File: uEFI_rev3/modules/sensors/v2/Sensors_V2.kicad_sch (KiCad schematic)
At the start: 12 parts, among them J1 Conn_01x05_Female, U1 LM321, U2 LM321

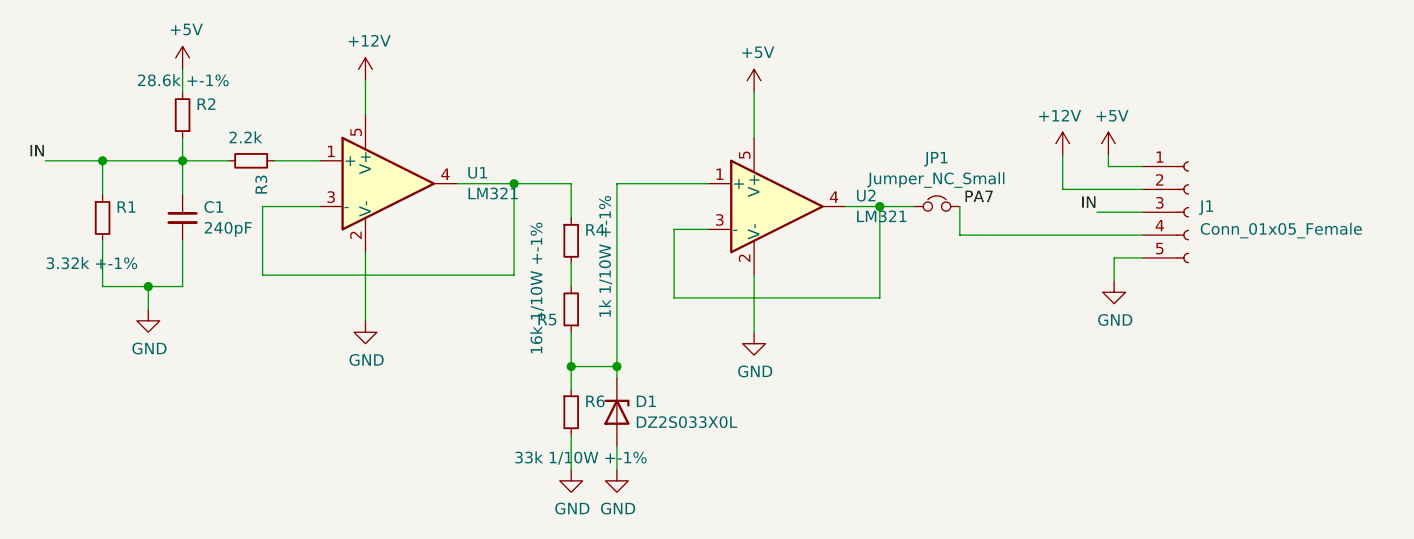
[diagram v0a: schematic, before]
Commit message: move old boards to __old
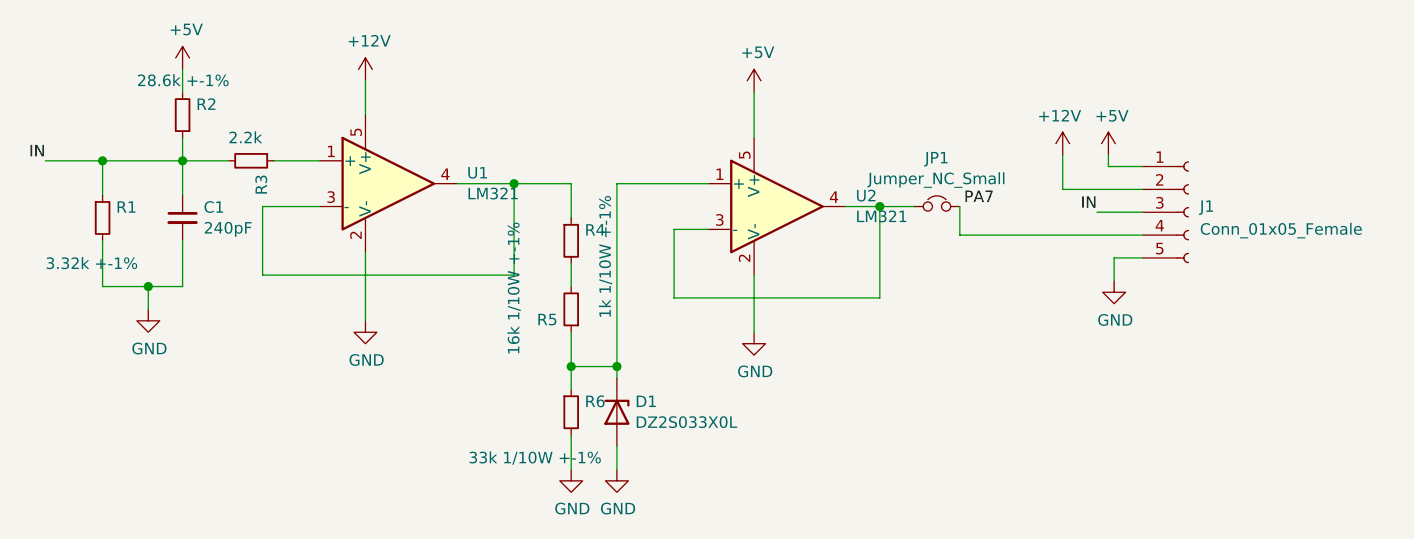
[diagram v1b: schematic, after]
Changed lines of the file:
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@@
-(kicad_sch (version 20210126) (generator eeschema)
+(kicad_sch (version 20210621) (generator eeschema)
   (paper "A4")
   (junction (at 82.55 82.55) (diameter 1.016) (color 0 0 0 0))
@@
       (effects (font (size 1.27 1.27)) (justify left))
     )
-    (property "Value" "16k 1/10W +-1%" (id 1) (at 130.81 104.14 90)
+    (property "Value" "16k 1/10W +-1%" (id 1) (at 128.27 104.14 90)
       (effects (font (size 1.27 1.27)) (justify left))
     )
@@
       (effects (font (size 1.27 1.27)) (justify left))
     )
-    (property "Value" "33k  1/10W +-1%" (id 1) (at 128.27 115.57 0)
-      (effects (font (size 1.27 1.27)) (justify left))
-    )
+    (property "Value" "33k  1/10W +-1%" (id 1) (at 123.19 115.57 0)
+      (effects (font (size 1.27 1.27)) (justify left))
+    )

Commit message: rev3, analog inputs
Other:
- note added: "Remove?"
